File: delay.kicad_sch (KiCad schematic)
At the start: 57 parts, among them J1 Footswitch_Terminal_01x02, J2 LED_Socket_01x02, J3 Footswitch_Terminal_Signal_01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, J4 Power_Supply_Terminal_01x02, J5 IO_Ground_Terminal_01x02, U1 L7805, U2 TL072, U3 PT2399

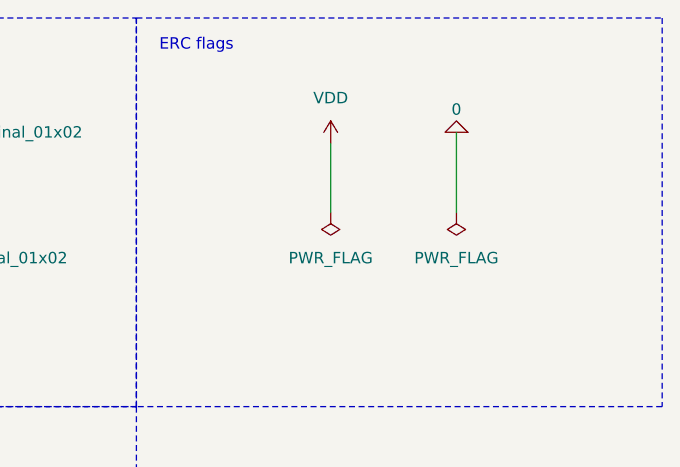
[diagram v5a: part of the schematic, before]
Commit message: add some connections (first draw)
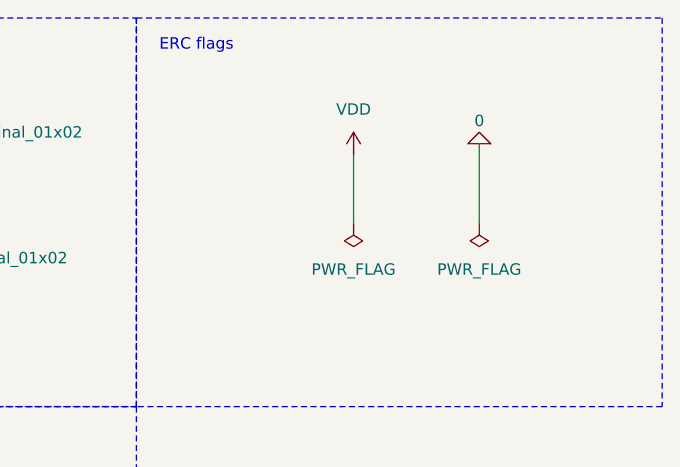
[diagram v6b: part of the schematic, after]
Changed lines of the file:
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@@
     (stroke (width 0) (type default))
   )
-  (wire (pts (xy 257.81 26.67) (xy 257.81 35.56))
+  (wire (pts (xy 260.35 27.94) (xy 260.35 36.83))
     (stroke (width 0) (type default))
   )
@@
     (stroke (width 0) (type default))
   )
-  (wire (pts (xy 243.84 27.94) (xy 243.84 35.56))
+  (wire (pts (xy 246.38 29.21) (xy 246.38 36.83))
     (stroke (width 0) (type default))
   )
@@
     )
   )
-  (symbol (lib_id "power:PWR_FLAG") (at 257.81 35.56 180) (unit 1)
+  (symbol (lib_id "power:PWR_FLAG") (at 260.35 36.83 180) (unit 1)
     (in_bom yes) (on_board yes) (dnp no) (fields_autoplaced)
-    (property "Reference" "#FLG02" (at 257.81 37.465 0)
-      (effects (font (size 1.27 1.27)) hide)
-    )
-    (property "Value" "PWR_FLAG" (at 257.81 40.64 0)
-      (effects (font (size 1.27 1.27)))
-    )
-    (property "Footprint" "" (at 257.81 35.56 0)
-      (effects (font (size 1.27 1.27)) hide)
-    )
-    (property "Datasheet" "~" (at 257.81 35.56 0)
+    (property "Reference" "#FLG02" (at 260.35 38.735 0)
+      (effects (font (size 1.27 1.27)) hide)
+    )
+    (property "Value" "PWR_FLAG" (at 260.35 41.91 0)
+      (effects (font (size 1.27 1.27)))
+    )
+    (property "Footprint" "" (at 260.35 36.83 0)
+      (effects (font (size 1.27 1.27)) hide)
+    )
+    (property "Datasheet" "~" (at 260.35 36.83 0)
       (effects (font (size 1.27 1.27)) hide)
     )
@@
     )
   )
-  (symbol (lib_id "Simulation_SPICE:0") (at 257.81 26.67 180) (unit 1)
-    (in_bom yes) (on_board yes) (dnp no)
-    (property "Reference" "#GND010" (at 257.81 24.13 0)
-      (effects (font (size 1.27 1.27)) hide)
-    )
-    (property "Value" "0" (at 257.81 24.13 0)
-      (effects (font (size 1.27 1.27)))
-    )
-    (property "Footprint" "" (at 257.81 26.67 0)
-      (effects (font (size 1.27 1.27)) hide)
-    )
-    (property "Datasheet" "~" (at 257.81 26.67 0)
+  (symbol (lib_id "Simulation_SPICE:0") (at 260.35 27.94 180) (unit 1)
+    (in_bom yes) (on_board yes) (dnp no)
+    (property "Reference" "#GND010" (at 260.35 25.4 0)
+      (effects (font (size 1.27 1.27)) hide)
+    )
+    (property "Value" "0" (at 260.35 25.4 0)
+      (effects (font (size 1.27 1.27)))
+    )
+    (property "Footprint" "" (at 260.35 27.94 0)
+      (effects (font (size 1.27 1.27)) hide)
+    )
+    (property "Datasheet" "~" (at 260.35 27.94 0)
       (effects (font (size 1.27 1.27)) hide)
     )
@@
     )
   )
-  (symbol (lib_id "power:PWR_FLAG") (at 243.84 35.56 180) (unit 1)
+  (symbol (lib_id "power:PWR_FLAG") (at 246.38 36.83 180) (unit 1)
     (in_bom yes) (on_board yes) (dnp no) (fields_autoplaced)
-    (property "Reference" "#FLG01" (at 243.84 37.465 0)
-      (effects (font (size 1.27 1.27)) hide)
-    )
-    (property "Value" "PWR_FLAG" (at 243.84 40.64 0)
-      (effects (font (size 1.27 1.27)))
-    )
-    (property "Footprint" "" (at 243.84 35.56 0)
-      (effects (font (size 1.27 1.27)) hide)
-    )
-    (property "Datasheet" "~" (at 243.84 35.56 0)
+    (property "Reference" "#FLG01" (at 246.38 38.735 0)
+      (effects (font (size 1.27 1.27)) hide)
+    )
+    (property "Value" "PWR_FLAG" (at 246.38 41.91 0)
+      (effects (font (size 1.27 1.27)))
+    )
+    (property "Footprint" "" (at 246.38 36.83 0)
+      (effects (font (size 1.27 1.27)) hide)
+    )
+    (property "Datasheet" "~" (at 246.38 36.83 0)
       (effects (font (size 1.27 1.27)) hide)
     )
@@
     )
   )
-  (symbol (lib_id "power:VDD") (at 243.84 27.94 0) (unit 1)
+  (symbol (lib_id "power:VDD") (at 246.38 29.21 0) (unit 1)
     (in_bom yes) (on_board yes) (dnp no) (fields_autoplaced)
-    (property "Reference" "#PWR02" (at 243.84 31.75 0)
-      (effects (font (size 1.27 1.27)) hide)
-    )
-    (property "Value" "VDD" (at 243.84 22.86 0)
-      (effects (font (size 1.27 1.27)))
-    )
-    (property "Footprint" "" (at 243.84 27.94 0)
-      (effects (font (size 1.27 1.27)) hide)
-    )
-    (property "Datasheet" "" (at 243.84 27.94 0)
-      (effects (font (size 1.27 1.27)) hide)
-    )
+    (property "Reference" "#PWR02" (at 246.38 33.02 0)
+      (effects (font (size 1.27 1.27)) hide)
+    )
+    (property "Value" "VDD" (at 246.38 24.13 0)
+      (effects (font (size 1.27 1.27)))
+    )
+    (property "Footprint" "" (at 246.38 29.21 0)
+      (effects (font (size 1.27 1.27)) hide)
+    )
+    (property "Datasheet" "" (at 246.38 29.21 0)
+      (effects (font (size 1.27 1.27)) hide)
+    )

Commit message: create connections for all signals except 0
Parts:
- U1: footprint Ic:TO255P460X1020X2008-3P -> Ic:L7805CD2T
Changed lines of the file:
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@@
       (effects (font (size 1.27 1.27)))
     )
-    (property "Footprint" "Ic:TO255P460X1020X2008-3P" (at 85.725 35.56 0)
+    (property "Footprint" "Ic:L7805CD2T" (at 85.725 35.56 0)
       (effects (font (size 1.27 1.27) italic) (justify left) hide)
     )

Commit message: add ground vias inside stabilisator GND field, add board revision info
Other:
- title: Delay guitar effect -> Delay Guitar Effect
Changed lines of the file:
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@@
   (paper "A4")
   (title_block
-    (title "Delay guitar effect")
-    (date "2023-11-05")
+    (title "Delay Guitar Effect")
+    (date "2023-11-24")
     (rev "1")
     (comment 1 "Dawid Stawiszyński")
